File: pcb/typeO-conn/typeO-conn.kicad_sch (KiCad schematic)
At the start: 9 parts, among them J1 USB_C_Receptacle_USB2.0, SW1 SW_DIP_x01

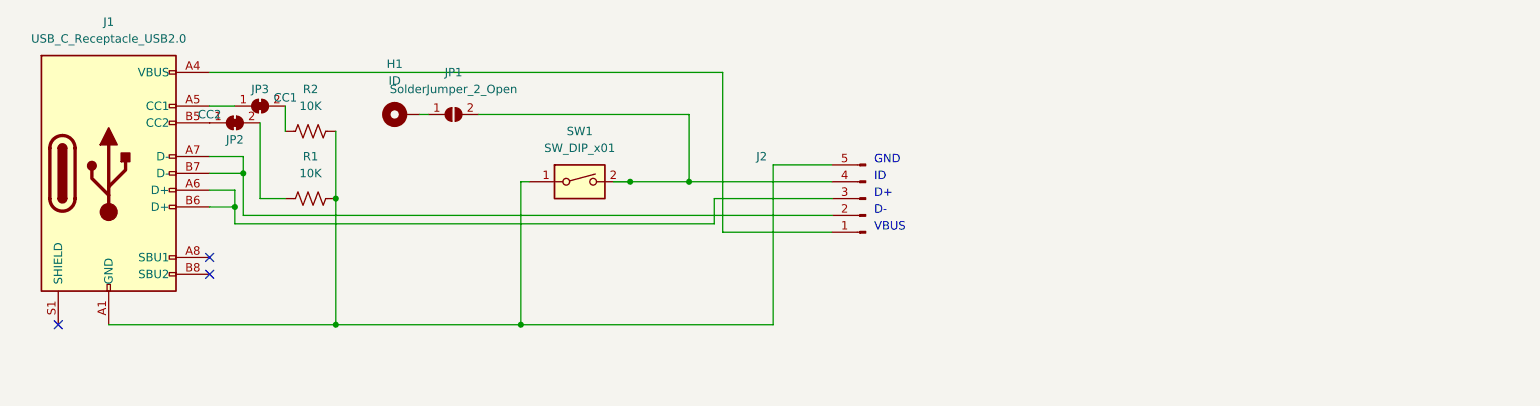
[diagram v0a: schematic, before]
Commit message: Change naming scheme for PCB design
Will start using git tags to mark versions and just have one file. Git
will save version history.
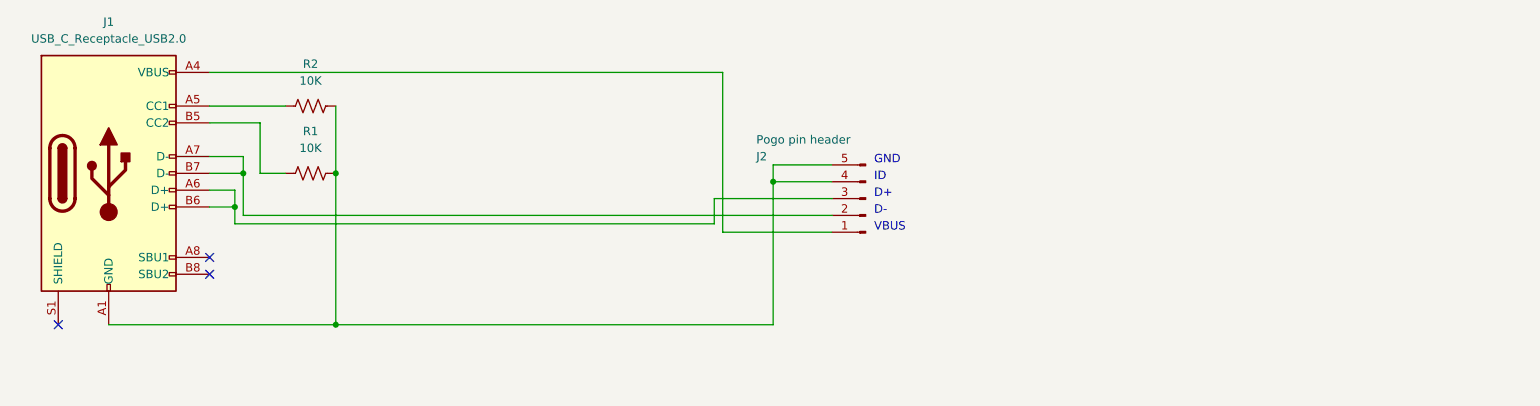
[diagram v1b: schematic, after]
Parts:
- removed H1: ID, Connector_Wire:SolderWire-0.1sqmm_1x01_D0.4mm_OD1mm, symbol Mechanical:MountingHole_Pad
- removed JP1: SolderJumper_2_Open, Jumper:SolderJumper-2_P1.3mm_Open_TrianglePad1.0x1.5mm, symbol Jumper:SolderJumper_2_Open
- removed JP2: CC2, Jumper:SolderJumper-2_P1.3mm_Bridged_RoundedPad1.0x1.5mm, symbol Jumper:SolderJumper_2_Bridged
- removed JP3: CC1, Jumper:SolderJumper-2_P1.3mm_Bridged_RoundedPad1.0x1.5mm, symbol Jumper:SolderJumper_2_Bridged
- removed SW1: SW_DIP_x01, Button_Switch_SMD:SW_DIP_SPSTx01_Slide_Omron_A6S-110x_W8.9mm_P2.54mm, symbol Switch:SW_DIP_x01
- J2: value (none) -> Pogo pin header; footprint (none) -> Connector_PinHeader_2.54mm:PinHeader_1x05_P2.54mm_Vertical
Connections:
- net at J1.A1 (GND), J1.A12 (GND), J1.B1 (GND)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: now also J2.4 (Pin_4)
- net at J1.A5 (CC1): now also R2.2
- net at J1.B5 (CC2): now also R1.2
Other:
- moved on the sheet: R1, R2

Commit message: Start work on typeO-conn v2
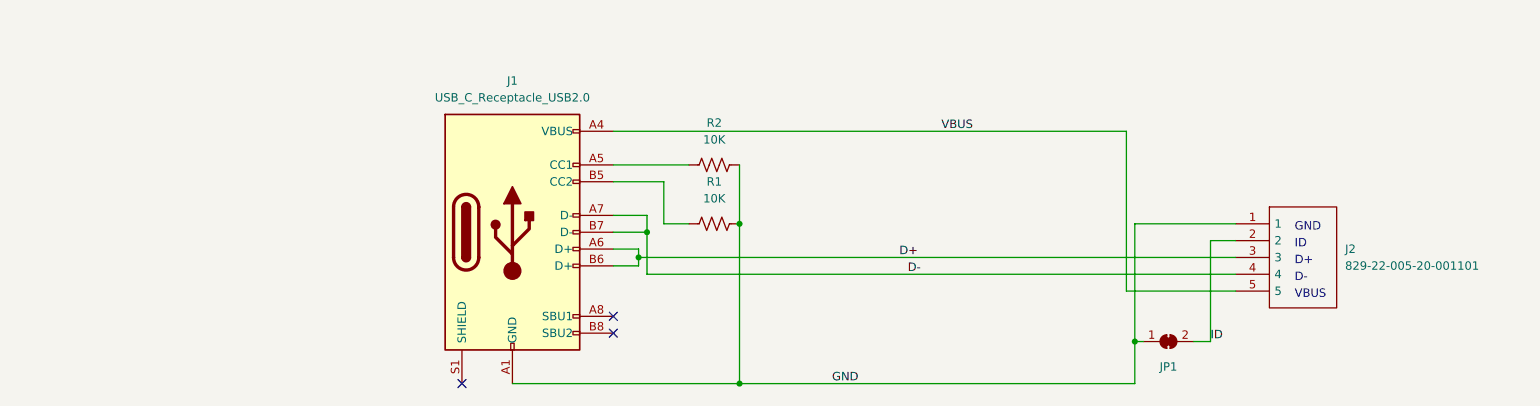
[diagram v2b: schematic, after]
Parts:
- removed J2: Pogo pin header, Connector_PinHeader_2.54mm:PinHeader_1x05_P2.54mm_Vertical, symbol Connector:Conn_01x05_Male
- added J2: 829-22-005-20-001101, 8292200520001101, symbol 829-22-005-20-001101 Pogo:829-22-005-20-001101
- added JP1: (no value), symbol Jumper:SolderJumper_2_Bridged
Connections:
- net GND: now reaches J1.A1 (GND), J1.A12 (GND), J1.B1 (GND), J1.B12 (GND), R1.1, R2.1
- net GND: now also J2.1, JP1.1 (A)
- net VBUS: now reaches J1.A4 (VBUS), J1.A9 (VBUS), J1.B4 (VBUS), J1.B9 (VBUS)
- net VBUS: now also J2.5
- net D+: now reaches J1.A6 (D+), J1.B6 (D+)
- net D+: now also J2.3
- net D-: now reaches J1.A7 (D-), J1.B7 (D-)
- net D-: now also J2.4
- new net ID: J2.2, JP1.2 (B)
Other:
- moved on the sheet: J1, R1, R2

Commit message: Prettify circuit diagram and add to Readme
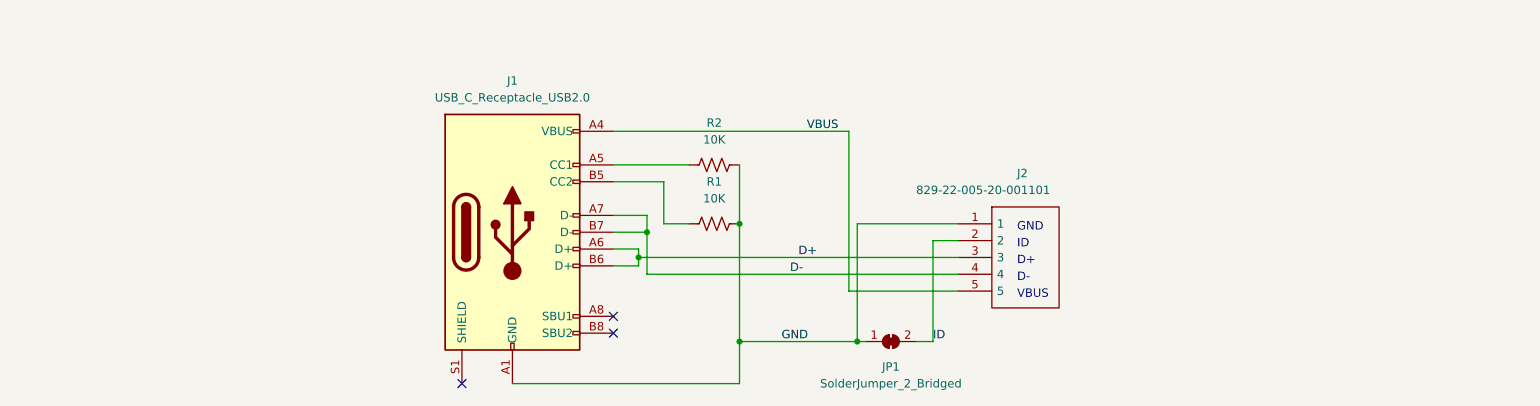
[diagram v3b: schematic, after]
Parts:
- JP1: value (none) -> SolderJumper_2_Bridged; footprint (none) -> Jumper:SolderJumper-2_P1.3mm_Open_TrianglePad1.0x1.5mm
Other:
- moved on the sheet: J2, JP1

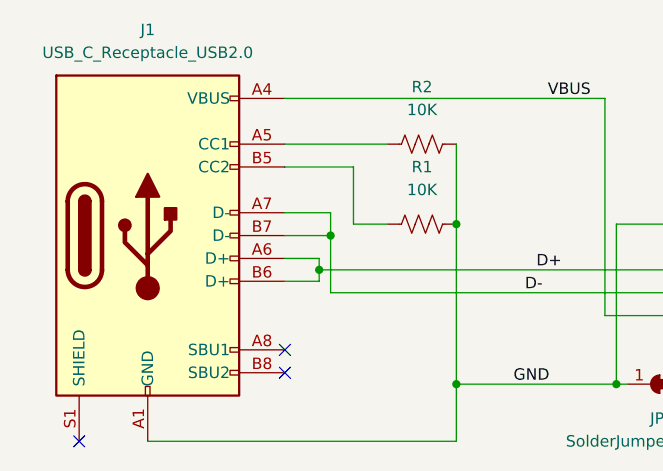
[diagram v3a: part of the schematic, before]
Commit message: Change resistor values
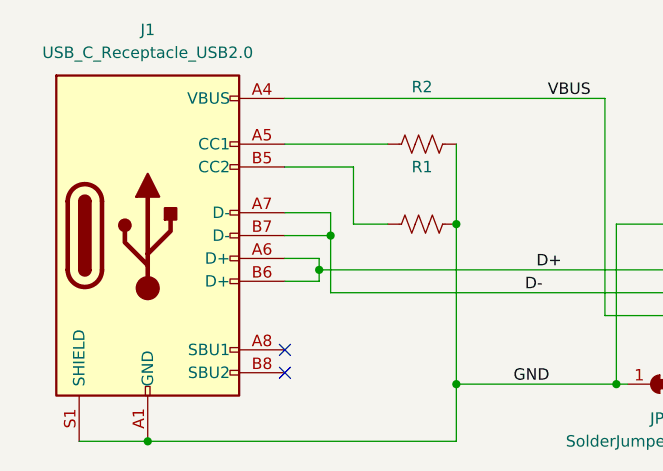
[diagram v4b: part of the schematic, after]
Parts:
- R1, R2: value 10K -> (none)
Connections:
- net GND: now also J1.S1 (SHIELD)
- no-connect marks 3 -> 2
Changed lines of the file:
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@@
   (junction (at 133.35 96.52) (diameter 0) (color 0 0 0 0)
+  )
+  (junction (at 99.06 120.65) (diameter 0) (color 0 0 0 0)
   )
   (junction (at 118.11 101.6) (diameter 0) (color 0 0 0 0)
@@
   (no_connect (at 114.3 110.49))
   (no_connect (at 114.3 113.03))
-  (no_connect (at 91.44 120.65))
   (wire (pts (xy 133.35 114.3) (xy 133.35 120.65))
     (stroke (width 0) (type default) (color 0 0 0 0))
@@
   )
   (wire (pts (xy 114.3 95.25) (xy 119.38 95.25))
+    (stroke (width 0) (type default) (color 0 0 0 0))
+  )
+  (wire (pts (xy 91.44 120.65) (xy 99.06 120.65))
     (stroke (width 0) (type default) (color 0 0 0 0))
   )
@@
     (in_bom yes) (on_board yes) (fields_autoplaced)
     (property "Reference" "R1" (id 0) (at 129.54 90.17 90))
-    (property "Value" "10K" (id 1) (at 129.54 92.71 90))
+    (property "Value" "" (id 1) (at 129.54 92.71 90))
     (property "Footprint" "Resistor_THT:R_Axial_DIN0207_L6.3mm_D2.5mm_P7.62mm_Horizontal" (id 2) (at 129.286 97.536 90)
       (effects (font (size 1.27 1.27)) hide)
@@
     (in_bom yes) (on_board yes) (fields_autoplaced)
     (property "Reference" "R2" (id 0) (at 129.54 81.28 90))
-    (property "Value" "10K" (id 1) (at 129.54 83.82 90))
+    (property "Value" "" (id 1) (at 129.54 83.82 90))
     (property "Footprint" "Resistor_THT:R_Axial_DIN0207_L6.3mm_D2.5mm_P7.62mm_Horizontal" (id 2) (at 129.286 88.646 90)
       (effects (font (size 1.27 1.27)) hide)
@@
     )
     (path "/7342cc82-e0e9-41f9-8b46-68197771b07f"
-      (reference "R1") (unit 1) (value "10K") (footprint "Resistor_THT:R_Axial_DIN0207_L6.3mm_D2.5mm_P7.62mm_Horizontal")
+      (reference "R1") (unit 1) (value "5.1k") (footprint "Resistor_THT:R_Axial_DIN0207_L6.3mm_D2.5mm_P7.62mm_Horizontal")
     )
     (path "/d78982c9-f3ac-4a5e-bbb4-2fd7f47d4ff6"
-      (reference "R2") (unit 1) (value "10K") (footprint "Resistor_THT:R_Axial_DIN0207_L6.3mm_D2.5mm_P7.62mm_Horizontal")
-    )
-  )
+      (reference "R2") (unit 1) (value "5.1k") (footprint "Resistor_THT:R_Axial_DIN0207_L6.3mm_D2.5mm_P7.62mm_Horizontal")
+    )
+  )
